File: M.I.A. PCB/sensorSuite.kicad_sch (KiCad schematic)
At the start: 13 parts, among them U3 MMC5983MA, U4 ICM-42688-P, U5 MS5611-01BA, U6 TMP117xxDRV, U7 MAX-M10S, U8 KX134-1211

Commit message: Worked on Layout, Changed IMU
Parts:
- removed U4: ICM-42688-P, Package_LGA:LGA-14_3x2.5mm_P0.5mm_LayoutBorder3x4y, symbol ICM-42688-P:ICM-42688-P
- added U4: ICM-45686, Package_LGA:Bosch_LGA-14_3x2.5mm_P0.5mm, symbol JLCImport:ICM-45686
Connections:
- net +3.3V: no longer C20.1, C21.1
- net GND: now also U4.6 (GND)
- net IMU_CS: now also U4.12 (AP_CS)
- net IMU_INT1: now also U4.4 (INT1/INT)
- net IMU_INT2: now also U4.9 (INT2/FSYNC/CLKIN)
- net SPI_MISO_SEN: now also U4.1 (AP_SDO/AP_AD0)
- net SPI_MOSI_SEN: now also U4.14 (AP_SDA/AP_SDIO/AP_SDI)
- net SPI_SCK_SEN: now also U4.13 (AP_SCL/AP_SCLK)
- new net: C20.1, U4.5 (VDDIO)
- new net: C21.1, U4.8 (VDD)
- no-connect marks 2 -> 6
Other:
- note added: "ICM-45686 6-Axis IMU"
- note removed: "ICM-42688 6-Axis IMU"

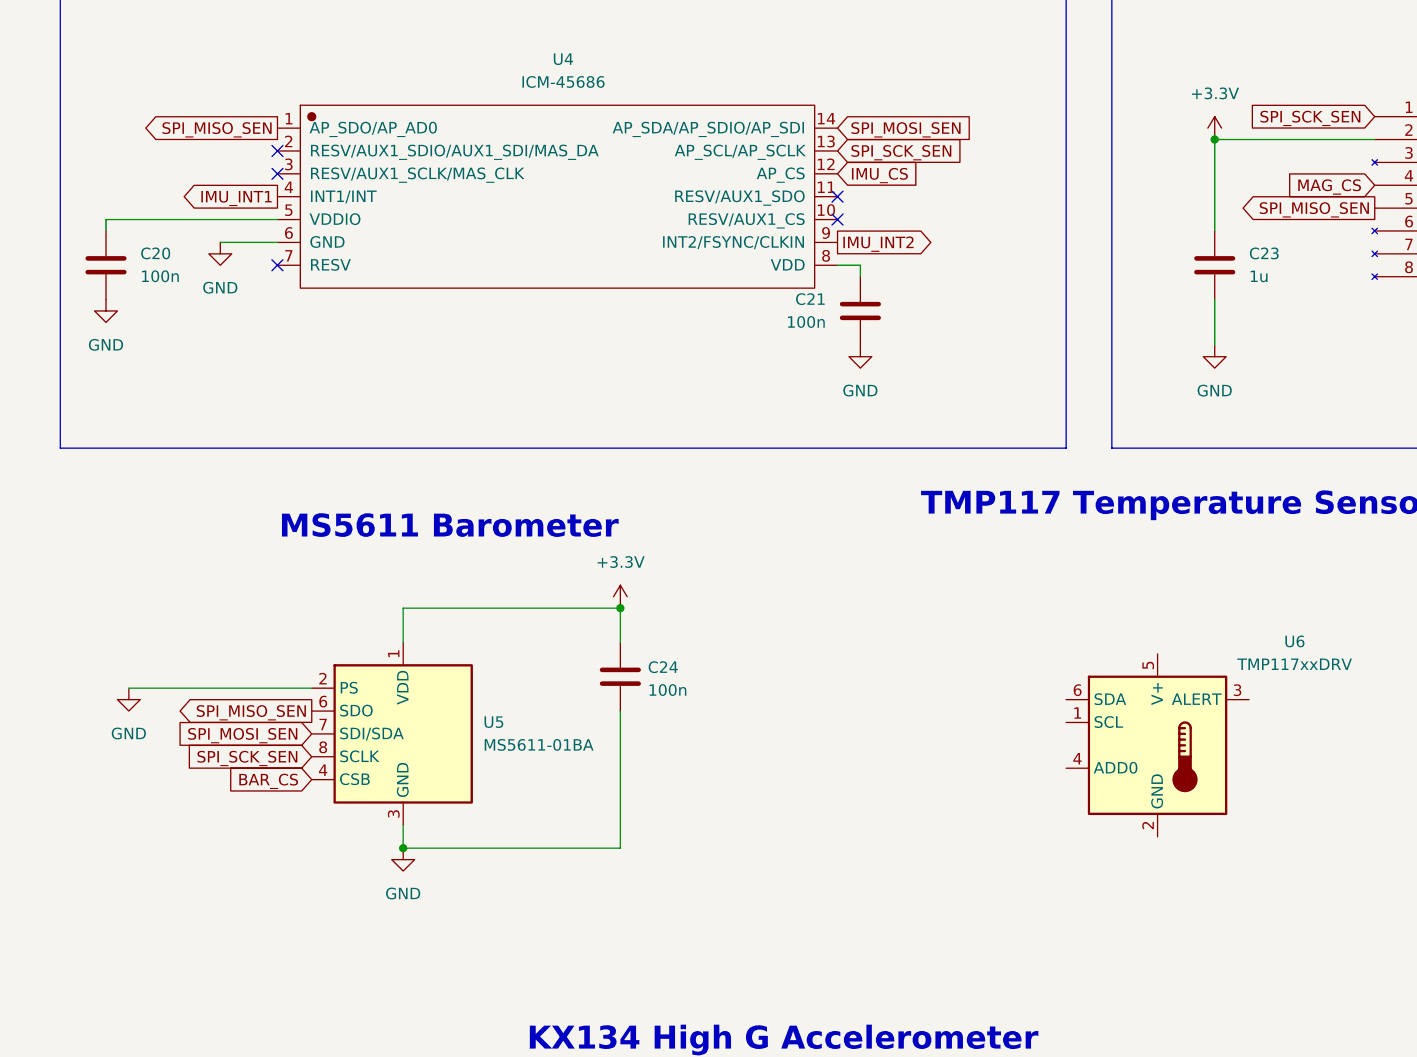
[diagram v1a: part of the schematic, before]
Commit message: Finished Layout other than gps, extra connectors, and ignition lines
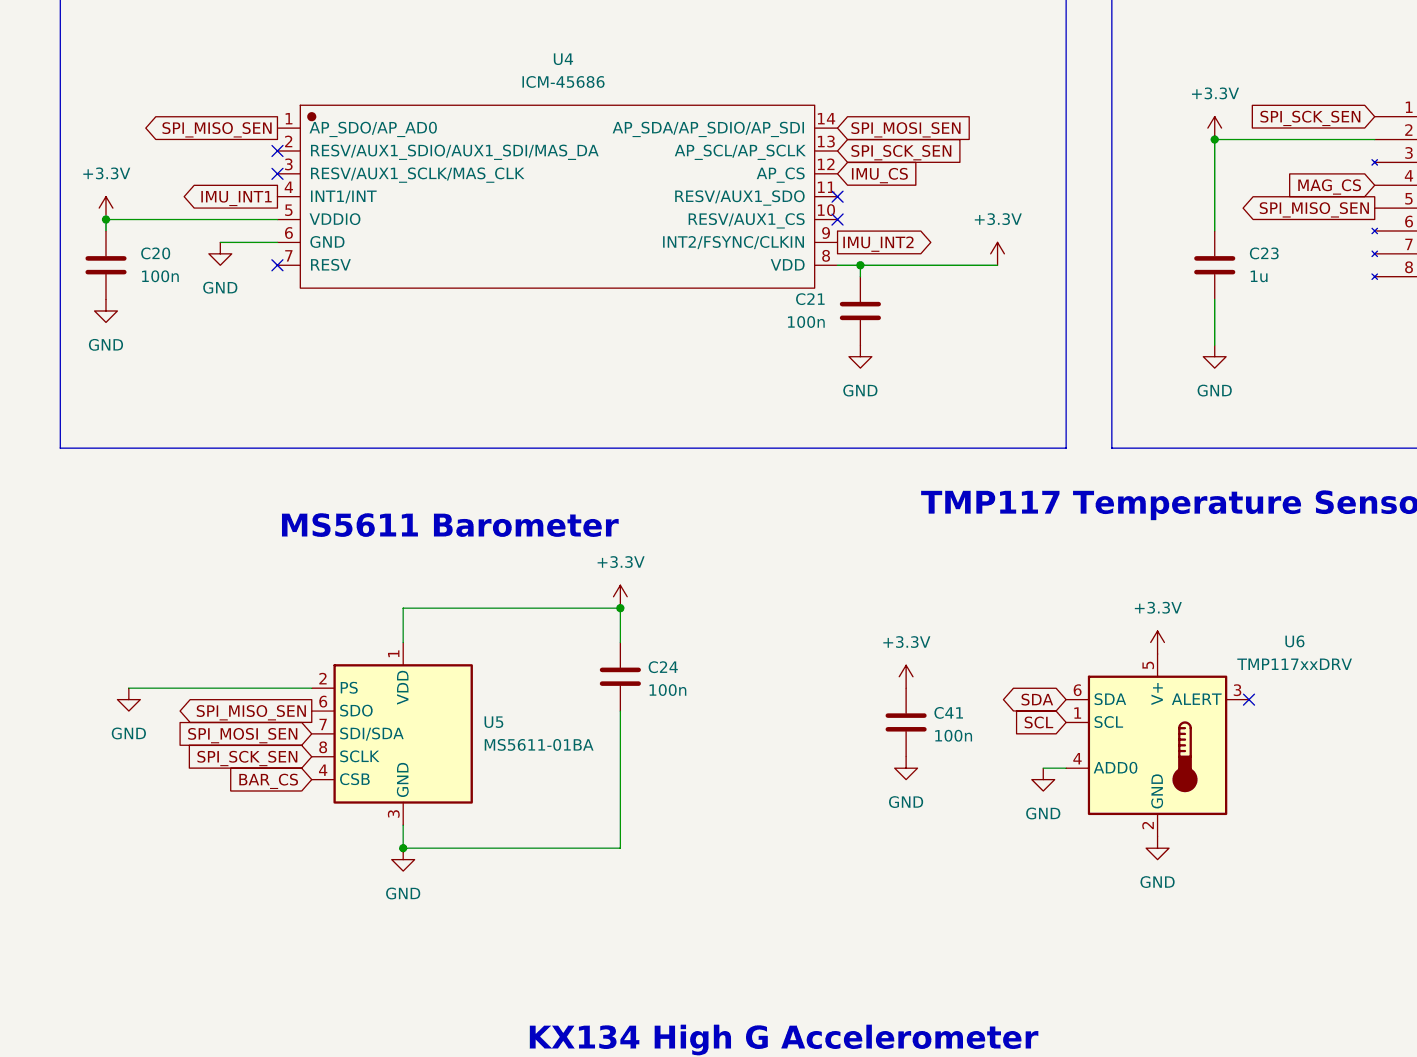
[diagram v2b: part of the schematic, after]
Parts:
- added C41: 100n, Capacitor_SMD:C_0603_1608Metric, symbol Device:C
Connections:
- net +3.3V: now also C20.1, C21.1, U4.5 (VDDIO), U4.8 (VDD), U6.5 (V+), C41.1
- net GND: now also U6.2 (GND), U6.4 (ADD0), C41.2
- net SCL: now reaches U6.1 (SCL)
- net SDA: now reaches U6.6 (SDA)
- no-connect marks 6 -> 7

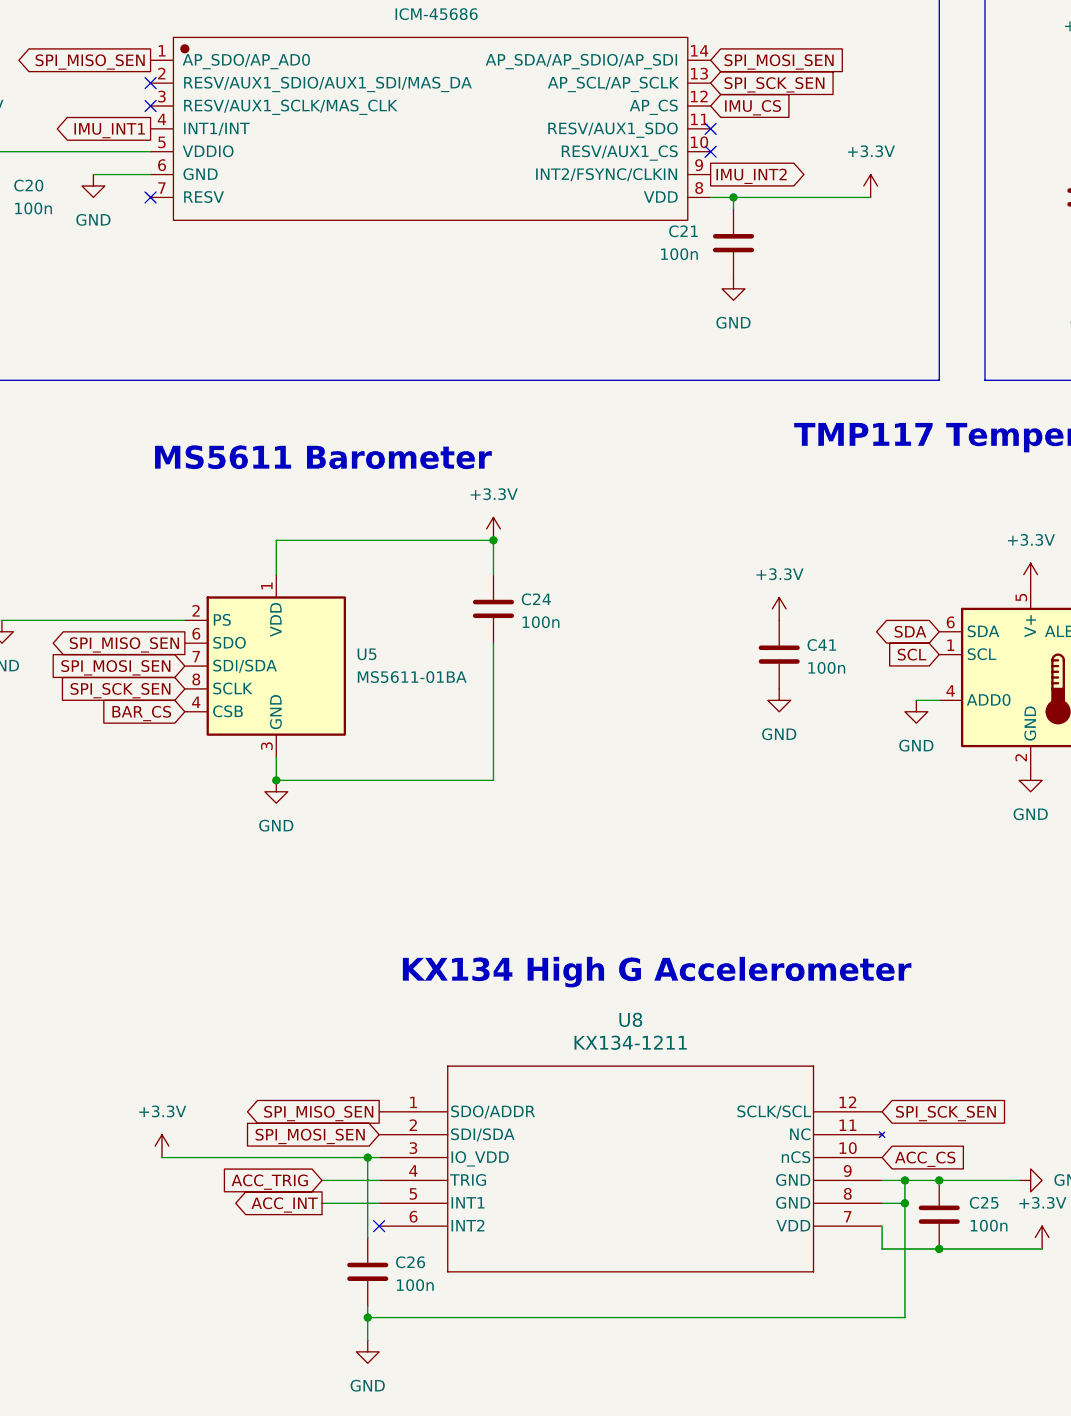
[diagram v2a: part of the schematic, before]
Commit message: Wired Sensors
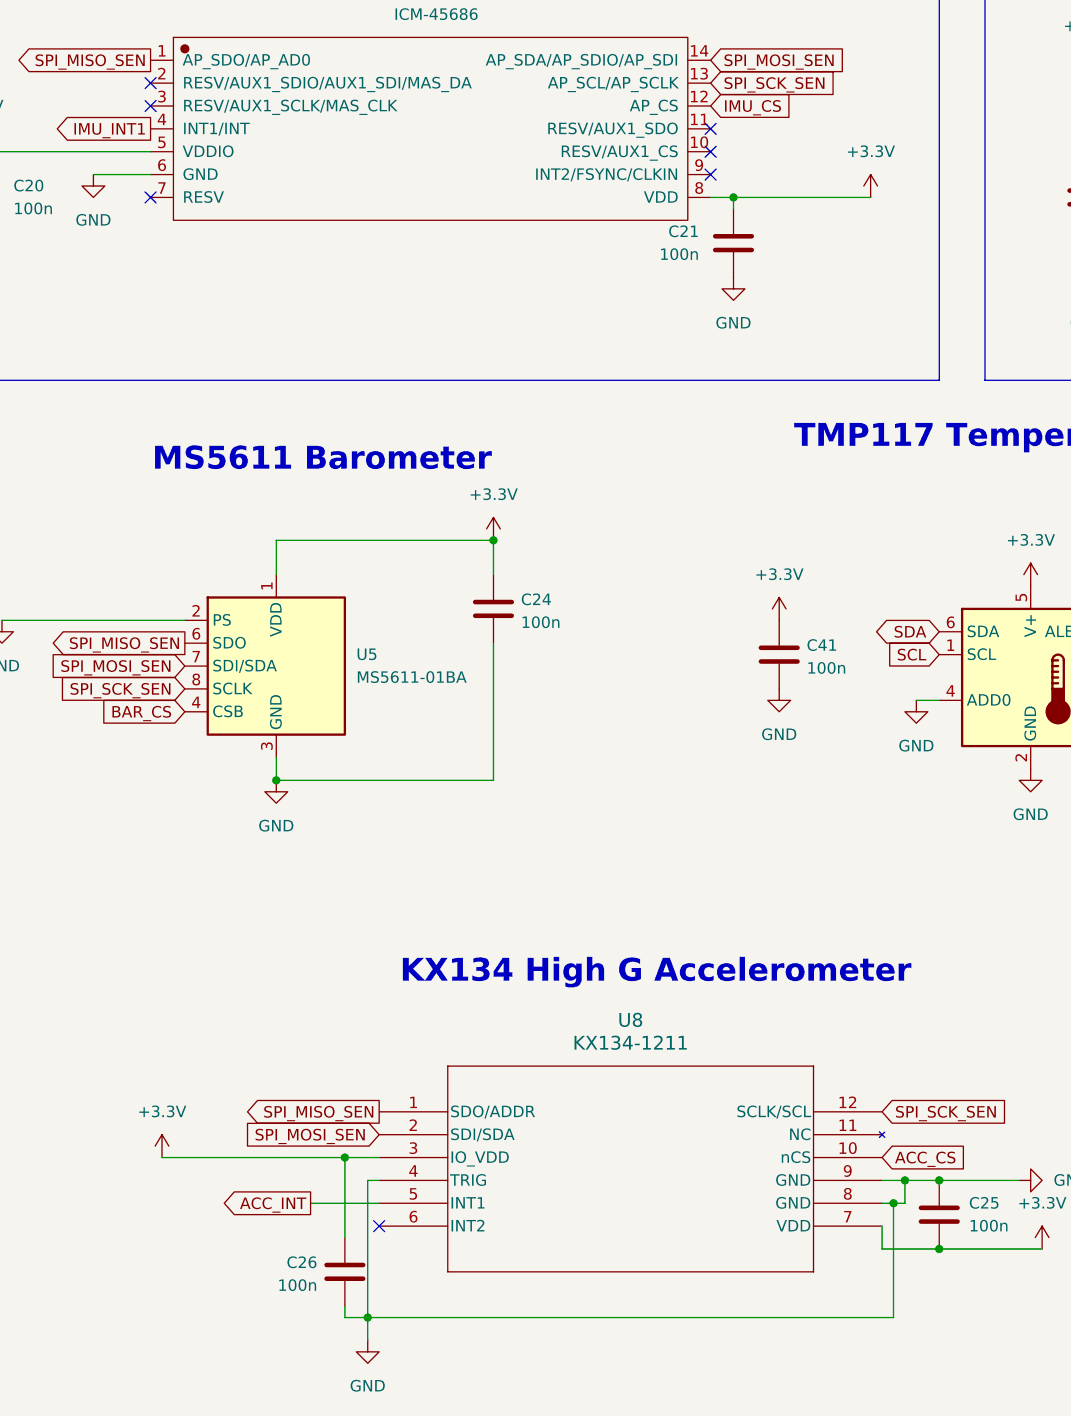
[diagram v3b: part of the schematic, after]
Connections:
- net ACC_TRIG is gone; now on net GND: U8.4 (TRIG)
- net IMU_INT2: no longer names the net of U4.9 (INT2/FSYNC/CLKIN)
- no-connect marks 7 -> 8
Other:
- moved on the sheet: C26
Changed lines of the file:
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@@
-	)
-	(junction
-		(at 63.5 158.75)
-		(diameter 0)
-		(color 0 0 0 0)
 	)
 	(junction
@@
 	)
 	(junction
-		(at 123.19 163.83)
-		(diameter 0)
-		(color 0 0 0 0)
-	)
-	(junction
 		(at 77.47 90.17)
 		(diameter 0)
@@
 	)
 	(junction
+		(at 60.96 158.75)
+		(diameter 0)
+		(color 0 0 0 0)
+	)
+	(junction
 		(at 143.51 38.1)
+		(diameter 0)
+		(color 0 0 0 0)
+	)
+	(junction
+		(at 121.92 163.83)
 		(diameter 0)
 		(color 0 0 0 0)
@@
 	)
 	(no_connect
-		(at 64.77 166.37)
+		(at 101.6 49.53)
 	)
 	(no_connect
@@
 		(at 101.6 44.45)
 	)
+	(no_connect
+		(at 64.77 166.37)
+	)
 	(wire
 		(pts
@@
 	(wire
 		(pts
-			(xy 123.19 176.53) (xy 123.19 163.83)
+			(xy 121.92 176.53) (xy 121.92 163.83)
 		)
 		(stroke
@@
 	(wire
 		(pts
-			(xy 58.42 163.83) (xy 64.77 163.83)
-		)
-		(stroke
-			(width 0)
-			(type default)
-		)
-	)
-	(wire
-		(pts
-			(xy 63.5 158.75) (xy 64.77 158.75)
-		)
-		(stroke
-			(width 0)
-			(type default)
-		)
-	)
-	(wire
-		(pts
-			(xy 63.5 176.53) (xy 123.19 176.53)
-		)
-		(stroke
-			(width 0)
-			(type default)
-		)
-	)
-	(wire
-		(pts
-			(xy 63.5 175.26) (xy 63.5 176.53)
+			(xy 60.96 158.75) (xy 64.77 158.75)
+		)
+		(stroke
+			(width 0)
+			(type default)
+		)
+	)
+	(wire
+		(pts
+			(xy 60.96 175.26) (xy 60.96 176.53)
 		)
 		(stroke
@@
 	(wire
 		(pts
+			(xy 57.15 163.83) (xy 64.77 163.83)
+		)
+		(stroke
+			(width 0)
+			(type default)
+		)
+	)
+	(wire
+		(pts
 			(xy 104.14 52.07) (xy 104.14 53.34)
 		)
@@
 	(wire
 		(pts
-			(xy 63.5 158.75) (xy 63.5 167.64)
+			(xy 60.96 158.75) (xy 60.96 167.64)
 		)
 		(stroke
@@
 	(wire
 		(pts
+			(xy 60.96 176.53) (xy 63.5 176.53)
+		)
+		(stroke
+			(width 0)
+			(type default)
+		)
+	)
+	(wire
+		(pts
 			(xy 119.38 52.07) (xy 104.14 52.07)
 		)
@@
 	(wire
 		(pts
+			(xy 63.5 161.29) (xy 63.5 176.53)
+		)
+		(stroke
+			(width 0)
+			(type default)
+		)
+	)
+	(wire
+		(pts
 			(xy 63.5 176.53) (xy 63.5 179.07)
 		)
@@
 	(wire
 		(pts
-			(xy 40.64 158.75) (xy 63.5 158.75)
+			(xy 40.64 158.75) (xy 60.96 158.75)
 		)
 		(stroke
@@
 	(wire
 		(pts
+			(xy 63.5 176.53) (xy 121.92 176.53)
+		)
+		(stroke
+			(width 0)
+			(type default)
+		)
+	)
+	(wire
+		(pts
 			(xy 127 161.29) (xy 135.89 161.29)
 		)
@@
 	(wire
 		(pts
-			(xy 120.65 163.83) (xy 123.19 163.83)
+			(xy 120.65 163.83) (xy 121.92 163.83)
 		)
 		(stroke
@@
 	(wire
 		(pts
-			(xy 58.42 161.29) (xy 64.77 161.29)
-		)
-		(stroke
-			(width 0)
-			(type default)
-		)
-	)
-	(wire
-		(pts
 			(xy 33.02 49.53) (xy 39.37 49.53)
 		)
@@
 	(wire
 		(pts
+			(xy 121.92 163.83) (xy 123.19 163.83)
+		)
+		(stroke
+			(width 0)
+			(type default)
+		)
+	)
+	(wire
+		(pts
 			(xy 242.57 50.8) (xy 247.65 50.8)
 		)
@@
 		(pts
 			(xy 120.65 168.91) (xy 127 168.91)
+		)
+		(stroke
+			(width 0)
+			(type default)
+		)
+	)
+	(wire
+		(pts
+			(xy 63.5 161.29) (xy 64.77 161.29)
 		)
 		(stroke
@@
 		)
 	)
-	(global_label "IMU_INT2"
-		(shape output)
-		(at 101.6 49.53 0)
-		(fields_autoplaced yes)
-		(effects
-			(font
-				(size 1.27 1.27)
-			)
-			(justify left)
-		)
-		(property "Intersheetrefs" "${INTERSHEET_REFS}"
-			(at 113.0519 49.53 0)
-			(effects
-				(font
-					(size 1.27 1.27)
-				)
-				(justify left)
-				(hide yes)
-			)
-		)
-	)
 	(global_label "SPI_MOSI_SEN"
 		(shape input)
@@
 	(global_label "ACC_INT"
 		(shape output)
-		(at 58.42 163.83 180)
-		(fields_autoplaced yes)
-		(effects
-			(font
-				(size 1.27 1.27)
-			)
-			(justify right)
-		)
-		(property "Intersheetrefs" "${INTERSHEET_REFS}"
-			(at 47.9357 163.83 0)
-			(effects
-				(font
-					(size 1.27 1.27)
-				)
-				(justify right)
-				(hide yes)
-			)
-		)
-	)
-	(global_label "ACC_TRIG"
-		(shape input)
-		(at 58.42 161.29 180)
-		(fields_autoplaced yes)
-		(effects
-			(font
-				(size 1.27 1.27)
-			)
-			(justify right)
-		)
-		(property "Intersheetrefs" "${INTERSHEET_REFS}"
-			(at 46.7262 161.29 0)
+		(at 57.15 163.83 180)
+		(fields_autoplaced yes)
+		(effects
+			(font
+				(size 1.27 1.27)
+			)
+			(justify right)
+		)
+		(property "Intersheetrefs" "${INTERSHEET_REFS}"
+			(at 46.6657 163.83 0)
 			(effects
 				(font
@@
 	(symbol
 		(lib_id "Device:C")
-		(at 63.5 171.45 0)
+		(at 60.96 171.45 0)
+		(mirror y)
 		(unit 1)
 		(exclude_from_sim no)
@@
 		(dnp no)
 		(property "Reference" "C26"
-			(at 66.548 170.434 0)
+			(at 57.912 170.434 0)
 			(effects
 				(font
@@
 		)
 		(property "Value" "100n"
-			(at 66.548 172.974 0)
+			(at 57.912 172.974 0)
 			(effects
 				(font
@@
 		)
 		(property "Footprint" "Capacitor_SMD:C_0603_1608Metric"
-			(at 64.4652 175.26 0)
+			(at 59.9948 175.26 0)
 			(effects
 				(font
@@
 		)
 		(property "Datasheet" "~"
-			(at 63.5 171.45 0)
+			(at 60.96 171.45 0)
 			(effects
 				(font
@@
 		)
 		(property "Description" "Ceramic Capacitor"
-			(at 63.5 171.45 0)
+			(at 60.96 171.45 0)
 			(effects
 				(font
@@
 		)
 		(property "Availability" ""
-			(at 63.5 171.45 0)
+			(at 60.96 171.45 0)
 			(effects
 				(font
@@
 		)
 		(property "Check_prices" ""
-			(at 63.5 171.45 0)
+			(at 60.96 171.45 0)
 			(effects
 				(font
@@
 		)
 		(property "Description_1" ""
-			(at 63.5 171.45 0)
+			(at 60.96 171.45 0)
 			(effects
 				(font
@@
 		)
 		(property "MANUFACTURER" ""
-			(at 63.5 171.45 0)
+			(at 60.96 171.45 0)
 			(effects
 				(font
@@
 		)
 		(property "MAXIMUM_PACKAGE_HEIGHT" ""
-			(at 63.5 171.45 0)
+			(at 60.96 171.45 0)
 			(effects
 				(font
@@
 		)
 		(property "MF" ""
-			(at 63.5 171.45 0)
+			(at 60.96 171.45 0)
 			(effects
 				(font
@@
 		)
 		(property "MP" ""
-			(at 63.5 171.45 0)
+			(at 60.96 171.45 0)
 			(effects
 				(font
@@
 		)
 		(property "PARTREV" ""
-			(at 63.5 171.45 0)
+			(at 60.96 171.45 0)
 			(effects
 				(font
@@
 		)
 		(property "Package" ""
-			(at 63.5 171.45 0)
+			(at 60.96 171.45 0)
 			(effects
 				(font
@@
 		)
 		(property "Price" ""
-			(at 63.5 171.45 0)
+			(at 60.96 171.45 0)
 			(effects
 				(font
@@
 		)
 		(property "Purchase-URL" ""
-			(at 63.5 171.45 0)
+			(at 60.96 171.45 0)
 			(effects
 				(font
@@
 		)
 		(property "STANDARD" ""
-			(at 63.5 171.45 0)
+			(at 60.96 171.45 0)
 			(effects
 				(font
@@
 		)
 		(property "SnapEDA_Link" ""
-			(at 63.5 171.45 0)
+			(at 60.96 171.45 0)
 			(effects
 				(font
@@
 		)
 		(property "JLCPCB Part #" ""
-			(at 63.5 171.45 0)
+			(at 60.96 171.45 0)
 			(effects
 				(font
@@
 		)
 		(property "Sim.Device" ""
-			(at 63.5 171.45 0)
+			(at 60.96 171.45 0)
 			(effects
 				(font
@@
 		)
 		(property "LCSC Part Number" "C1525"
-			(at 63.5 171.45 0)
+			(at 60.96 171.45 0)
 			(effects
 				(font
@@
 		)
 		(property "LCSC" ""
-			(at 63.5 171.45 0)
+			(at 60.96 171.45 0)
 			(effects
 				(font
@@
 		)
 		(property "Manufacturer" ""
-			(at 63.5 171.45 0)
+			(at 60.96 171.45 0)
 			(effects
 				(font
@@
 		)
 		(property "Manufacturer Part" ""
-			(at 63.5 171.45 0)
-			(effects
-				(font
+			(at 60.96 171.45 0)
+			(effects
+				(font
